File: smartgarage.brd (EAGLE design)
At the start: 24.7 x 66 mm, 18 parts, among them J1 USB_MINI-B_SMT, J2 CLOSED_REED, J3 IN, J4 OUT, J5 PROG, J6 OPEN_REED, U2 ESP-12F

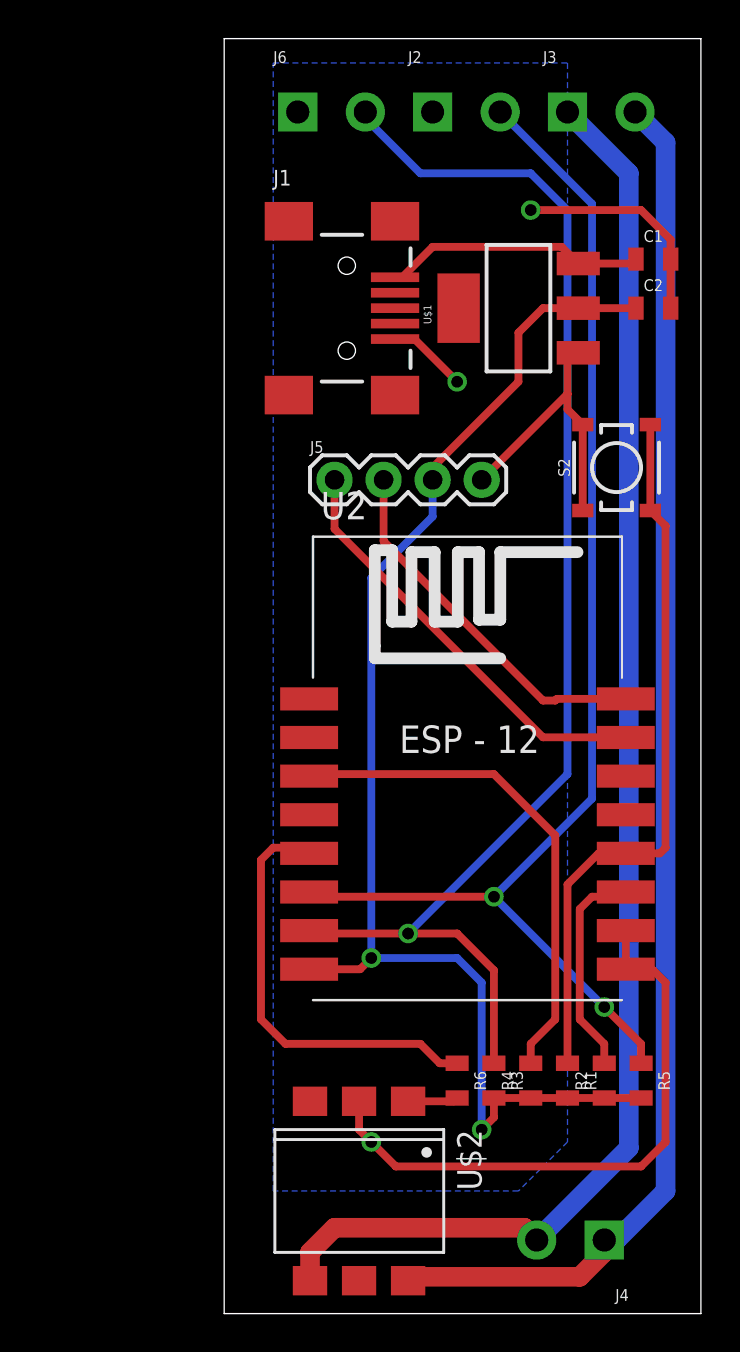
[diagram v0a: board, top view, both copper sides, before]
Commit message: V1.2 - Rotated ESP, add lock
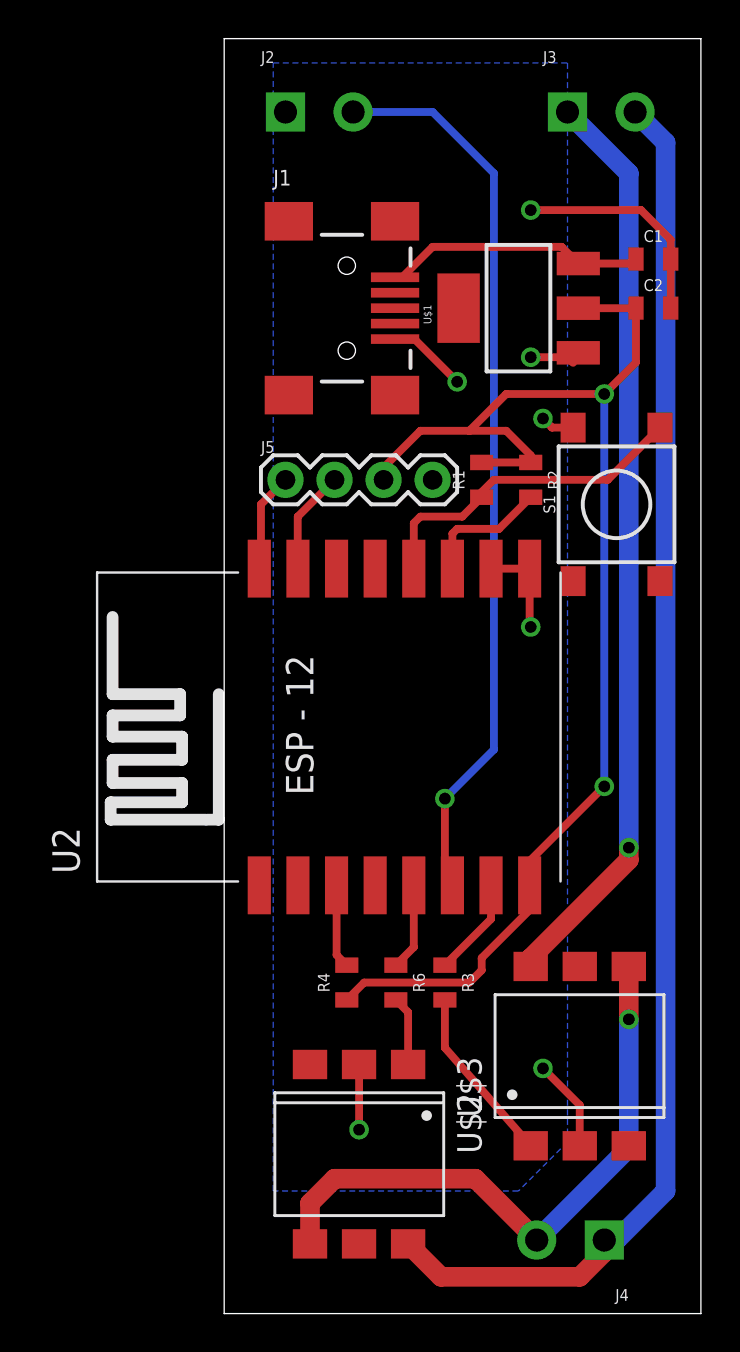
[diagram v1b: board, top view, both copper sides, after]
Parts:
- removed J6: OPEN_REED, SparkFun-Connectors:SCREWTERMINAL-3.5MM-2-NS
- removed R5: 10K, SparkFun-Resistors:0805
- removed S2: MOMENTARY-SWITCH-SPST-SMD-4.5MM, SparkFun-Switches:TACTILE_SWITCH_SMD_4.5MM
- added S1: MOMENTARY-SWITCH-SPST-SMD-6.2MM-TALL, SparkFun-Switches:TACTILE_SWITCH_SMD_6.2MM_TALL
- added U$3: LH1546, smartgarage:DIL6-SMD
- R3: value 10K -> 100
- moved R1 31.4 mm to (13.3, 43.2), turned to 90 degrees
- moved R2 31.3 mm to (15.9, 43.2), turned to 270 degrees
- moved R4 10.8 mm to (6.35, 17.1)
- moved J2 7.62 mm to (3.17, 62.2)
- moved U2 6.75 mm to (7.62, 30.5), turned to 90 degrees
- moved R6 5.99 mm to (8.89, 17.1)
- moved R3 5.68 mm to (11.4, 17.1)
- moved J5 2.54 mm to (3.17, 43.2)
- moved U$2 1.91 mm to (6.99, 8.26)
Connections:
- removed net N$3: J3.1, J4.2, U$2.4
- new net N$7: R3.2, U$3.1
- new net N$8: J3.1, U$3.6
- new net N$9: J4.2, U$2.4, U$3.4
- net 3.3V: no longer R3.2, R5.2
- net GND: now also S1.B2, U$3.2; no longer J6.1, S2.1, S2.4
- net GPIO12: no longer R5.1
- net GPIO13: no longer J6.2
- net N$1: now also S1.A2; no longer S2.2, S2.3
- net RX: now also J5.2; no longer J5.1
- net TX: now also J5.1; no longer J5.2
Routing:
- net N$3: track 75.7 -> 0.00 mm
- net GPIO13: track 68.9 -> 5.12 mm, vias 1 -> 0
- net N$8: track 0.00 -> 47.7 mm, vias 0 -> 1
- net N$9: track 0.00 -> 31.8 mm, vias 0 -> 1
- net GND: track 62.9 -> 34.9 mm, vias 3 -> 7
- net N$4: track 26.4 -> 4.35 mm
- net N$1: track 37.4 -> 17.3 mm
- net GPIO12: track 66.2 -> 48.1 mm, vias 2 -> 1
- net GPIO14: track 22.2 -> 4.52 mm
- net RX: track 22.1 -> 5.39 mm
- net TX: track 19.2 -> 5.16 mm
- net N$7: track 0.00 -> 9.23 mm
- net N$5: track 11.3 -> 6.65 mm
- net 3.3V: track 69.0 -> 68.5 mm
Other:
- board text added: "SmartGarage v1.2"
- board text removed: "SmartGarage v1.1"

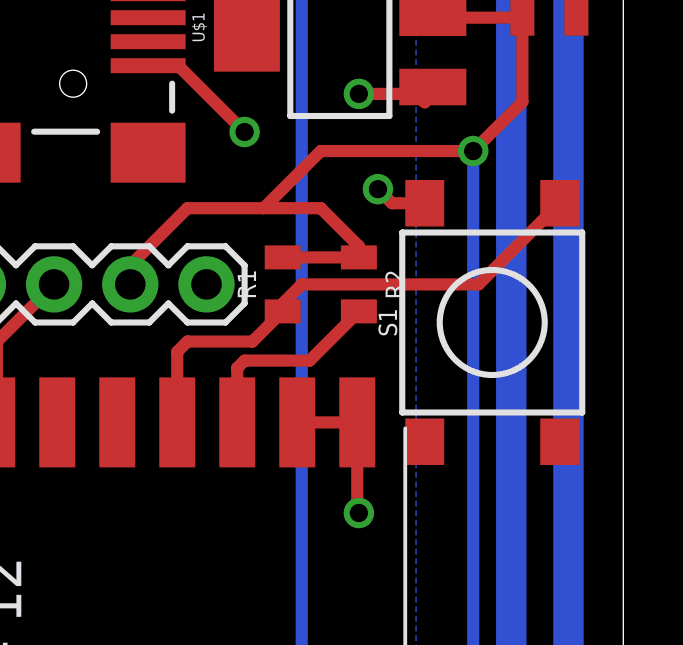
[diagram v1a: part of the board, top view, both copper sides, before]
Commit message: Adding firmward to project
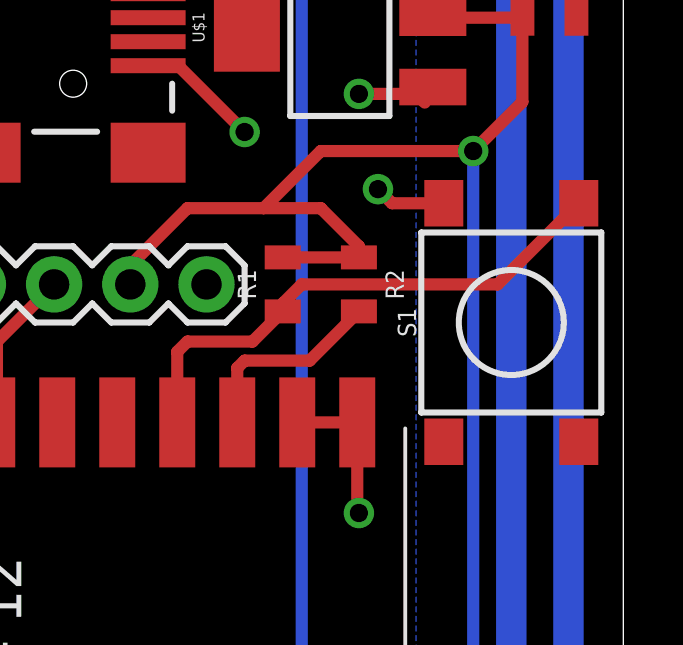
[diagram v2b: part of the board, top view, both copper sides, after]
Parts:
- moved S1 0.63 mm to (21.0, 41.9)
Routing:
- net GND: track 34.9 -> 35.5 mm
- net N$1: track 17.3 -> 17.9 mm
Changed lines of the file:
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@@
 </element>
 <element name="U$3" library="smartgarage" package="DIL6-SMD" value="LH1546" x="18.415" y="13.335"/>
-<element name="S1" library="SparkFun-Switches" package="TACTILE_SWITCH_SMD_6.2MM_TALL" value="MOMENTARY-SWITCH-SPST-SMD-6.2MM-TALL" x="20.32" y="41.91" rot="R90">
-<attribute name="SF_SKU" value="COM-12992" x="20.32" y="41.91" size="1.778" layer="27" rot="R90" display="off"/>
-<attribute name="PROD_ID" value="SWCH-11966" x="20.32" y="41.91" size="1.778" layer="27" rot="R90" display="off"/>
+<element name="S1" library="SparkFun-Switches" package="TACTILE_SWITCH_SMD_6.2MM_TALL" value="MOMENTARY-SWITCH-SPST-SMD-6.2MM-TALL" x="20.955" y="41.91" rot="R90">
+<attribute name="SF_SKU" value="COM-12992" x="20.955" y="41.91" size="1.778" layer="27" rot="R90" display="off"/>
+<attribute name="PROD_ID" value="SWCH-11966" x="20.955" y="41.91" size="1.778" layer="27" rot="R90" display="off"/>
 </element>
 </elements>
@@
 <wire x1="18.07" y1="49.24" x2="17.78" y2="49.53" width="0.4064" layer="1"/>
 <via x="16.51" y="46.355" extent="1-16" drill="0.6096"/>
-<wire x1="18.07" y1="45.885" x2="16.98" y2="45.885" width="0.4064" layer="1"/>
+<wire x1="18.705" y1="45.885" x2="16.98" y2="45.885" width="0.4064" layer="1"/>
 <wire x1="16.98" y1="45.885" x2="16.51" y2="46.355" width="0.4064" layer="1"/>
 </signal>
@@
 <wire x1="13.335" y1="42.28" x2="13.335" y2="42.545" width="0.4064" layer="1"/>
 <wire x1="13.335" y1="42.545" x2="13.97" y2="43.18" width="0.4064" layer="1"/>
-<wire x1="13.97" y1="43.18" x2="19.865" y2="43.18" width="0.4064" layer="1"/>
-<wire x1="19.865" y1="43.18" x2="22.57" y2="45.885" width="0.4064" layer="1"/>
+<wire x1="13.97" y1="43.18" x2="20.5" y2="43.18" width="0.4064" layer="1"/>
+<wire x1="20.5" y1="43.18" x2="23.205" y2="45.885" width="0.4064" layer="1"/>
 </signal>
 <signal name="N$4">

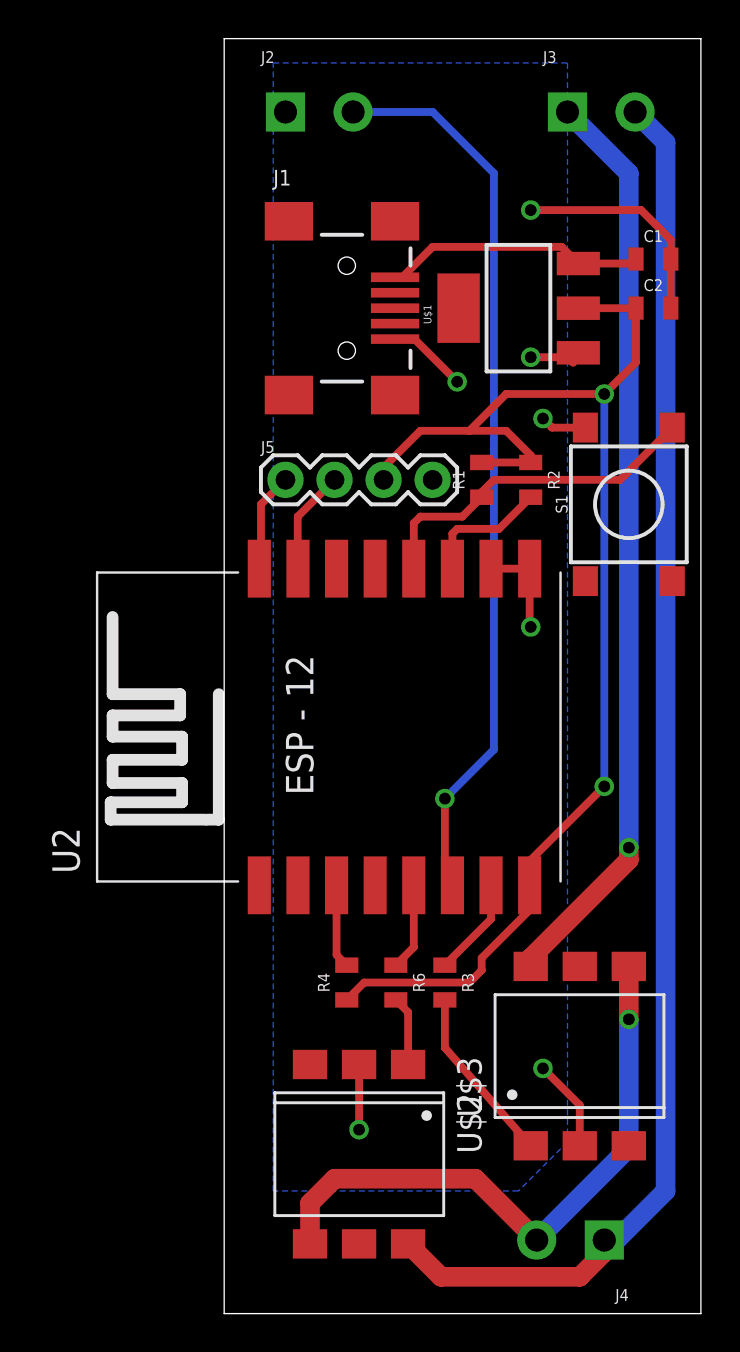
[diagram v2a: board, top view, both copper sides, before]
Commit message: Hardware 1.2.1, moved screw terminal
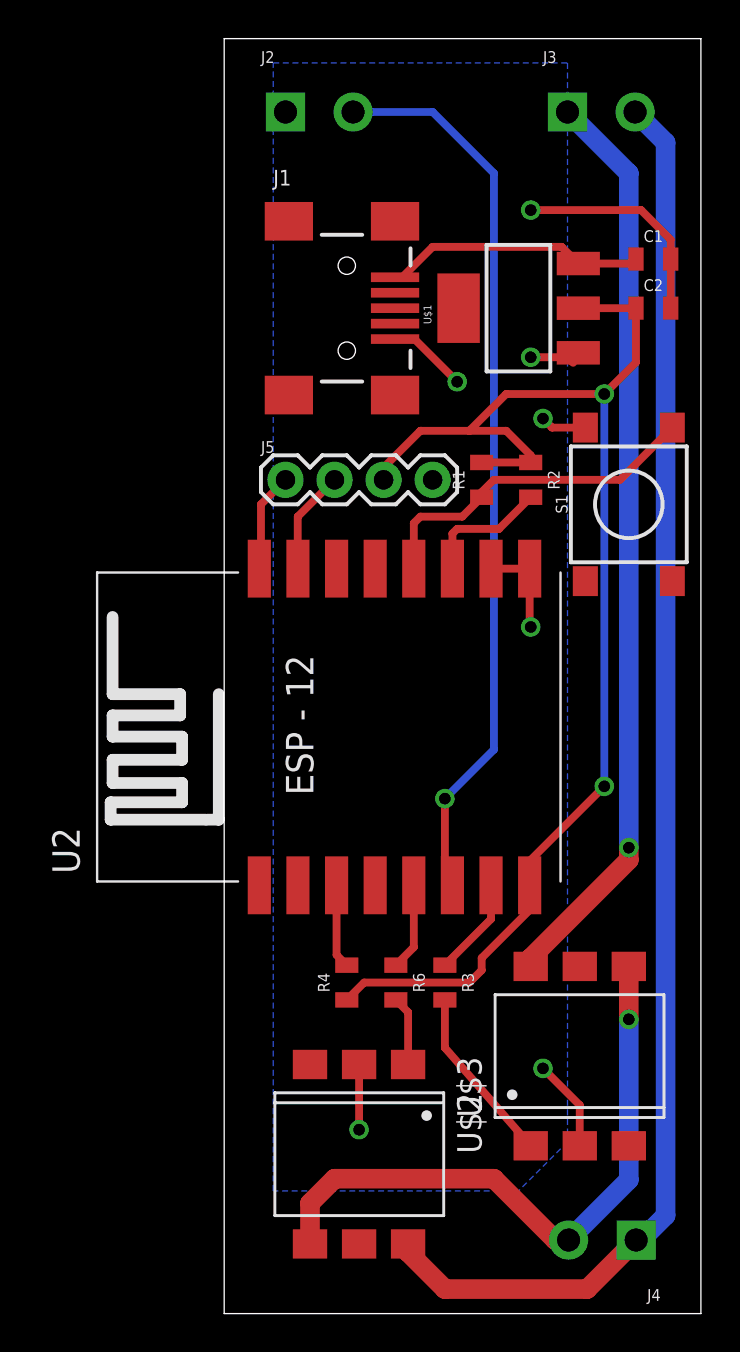
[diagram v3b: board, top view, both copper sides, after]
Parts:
- moved J4 1.65 mm to (21.3, 3.81)
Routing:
- net N$6: track 72.8 -> 73.9 mm
- net N$9: track 31.8 -> 32.8 mm
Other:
- board text added: "SmartGarage v1.2.1"
- board text removed: "SmartGarage v1.2"
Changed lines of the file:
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@@
 <wire x1="24.689" y1="66.03" x2="0" y2="66.03" width="0" layer="20"/>
 <wire x1="0" y1="66.03" x2="0" y2="0" width="0" layer="20"/>
-<text x="22.86" y="40.64" size="1.778" layer="22" rot="MR270">SmartGarage v1.2</text>
+<text x="22.86" y="40.64" size="1.778" layer="22" rot="MR270">SmartGarage v1.2.1</text>
 </plain>
 <attributes>
@@
 <attribute name="PROD_ID" value="CONN-08399" x="17.78" y="62.23" size="1.778" layer="27" display="off"/>
 </element>
-<element name="J4" library="SparkFun-Connectors" package="SCREWTERMINAL-3.5MM-2-NS" value="OUT" x="19.685" y="3.81" rot="R180">
-<attribute name="PROD_ID" value="CONN-08399" x="19.685" y="3.81" size="1.778" layer="27" rot="R180" display="off"/>
+<element name="J4" library="SparkFun-Connectors" package="SCREWTERMINAL-3.5MM-2-NS" value="OUT" x="21.336" y="3.81" rot="R180">
+<attribute name="PROD_ID" value="CONN-08399" x="21.336" y="3.81" size="1.778" layer="27" rot="R180" display="off"/>
 </element>
 <element name="J5" library="SparkFun-Connectors" package="1X04" value="PROG" x="3.175" y="43.18">
@@
 <signal name="N$6">
 <contactref element="J4" pad="1"/>
-<wire x1="22.86" y1="60.65" x2="22.86" y2="6.35" width="1.016" layer="16"/>
-<wire x1="22.86" y1="6.35" x2="20.32" y2="3.81" width="1.016" layer="16"/>
-<wire x1="20.32" y1="3.81" x2="19.685" y2="3.81" width="1.016" layer="16"/>
+<wire x1="22.86" y1="60.65" x2="22.86" y2="5.08" width="1.016" layer="16"/>
 <contactref element="U$2" pad="6"/>
 <contactref element="J3" pad="2"/>
 <wire x1="22.86" y1="60.65" x2="21.28" y2="62.23" width="1.016" layer="16"/>
-<wire x1="9.525" y1="3.61" x2="11.23" y2="1.905" width="1.016" layer="1"/>
-<wire x1="11.23" y1="1.905" x2="18.415" y2="1.905" width="1.016" layer="1"/>
-<wire x1="18.415" y1="1.905" x2="19.685" y2="3.175" width="1.016" layer="1"/>
-<wire x1="19.685" y1="3.175" x2="19.685" y2="3.81" width="1.016" layer="1"/>
+<wire x1="9.525" y1="3.61" x2="9.525" y2="3.175" width="1.016" layer="1"/>
+<wire x1="9.525" y1="3.175" x2="11.43" y2="1.27" width="1.016" layer="1"/>
+<wire x1="11.43" y1="1.27" x2="18.796" y2="1.27" width="1.016" layer="1"/>
+<wire x1="18.796" y1="1.27" x2="21.336" y2="3.81" width="1.016" layer="1"/>
+<wire x1="21.336" y1="3.81" x2="21.59" y2="3.81" width="1.016" layer="16"/>
+<wire x1="21.59" y1="3.81" x2="22.86" y2="5.08" width="1.016" layer="16"/>
 </signal>
 <signal name="N$5">
@@
 <contactref element="U$2" pad="4"/>
 <via x="20.955" y="15.24" extent="1-16" drill="0.6096" shape="square"/>
-<wire x1="20.955" y1="8.58" x2="16.185" y2="3.81" width="1.016" layer="16"/>
 <wire x1="20.955" y1="17.98" x2="20.955" y2="15.24" width="1.016" layer="1"/>
-<wire x1="20.955" y1="15.24" x2="20.955" y2="8.58" width="1.016" layer="16"/>
+<wire x1="20.955" y1="15.24" x2="20.955" y2="6.929" width="1.016" layer="16"/>
 <wire x1="4.445" y1="3.61" x2="4.445" y2="5.715" width="1.016" layer="1"/>
 <wire x1="4.445" y1="5.715" x2="5.715" y2="6.985" width="1.016" layer="1"/>
-<wire x1="5.715" y1="6.985" x2="13.01" y2="6.985" width="1.016" layer="1"/>
-<wire x1="13.01" y1="6.985" x2="16.185" y2="3.81" width="1.016" layer="1"/>
+<wire x1="5.715" y1="6.985" x2="13.97" y2="6.985" width="1.016" layer="1"/>
+<wire x1="20.955" y1="6.929" x2="17.836" y2="3.81" width="1.016" layer="16"/>
+<wire x1="17.836" y1="3.81" x2="17.145" y2="3.81" width="1.016" layer="1"/>
+<wire x1="17.145" y1="3.81" x2="13.97" y2="6.985" width="1.016" layer="1"/>
 </signal>
 </signals>
